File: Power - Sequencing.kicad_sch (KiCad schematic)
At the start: 0 parts

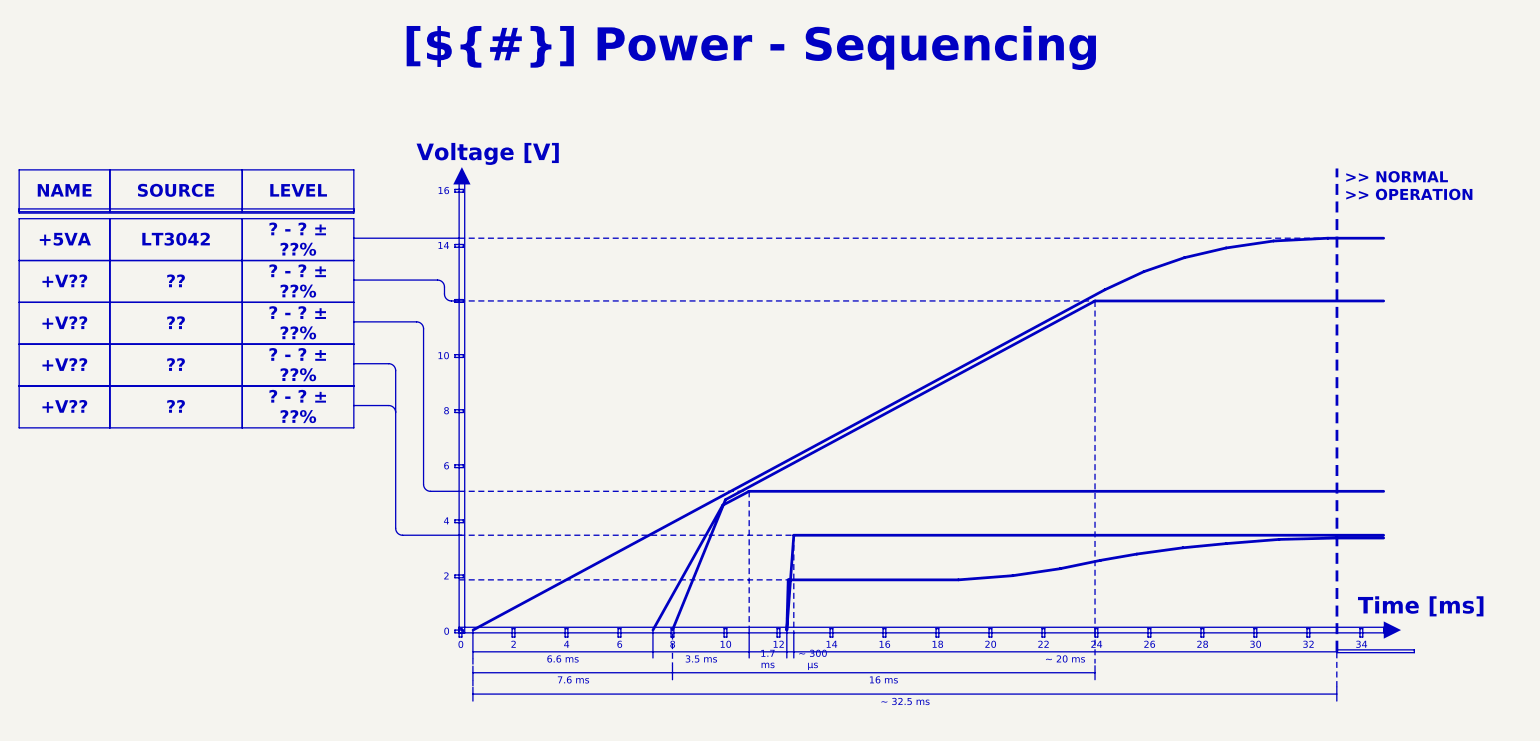
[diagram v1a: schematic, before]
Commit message: Fill template pages: block diagram, power sequencing, notes, revision history
Block Diagram and Power - Sequencing rebuilt from the real design (values computed
from the schematic); cover-page design notes, connector pinout notes, title-block
references; kicad-mcp-pro MCP config (.mcp.json).

Co-Authored-By: Claude Opus 5.5 <noreply@anthropic.com>
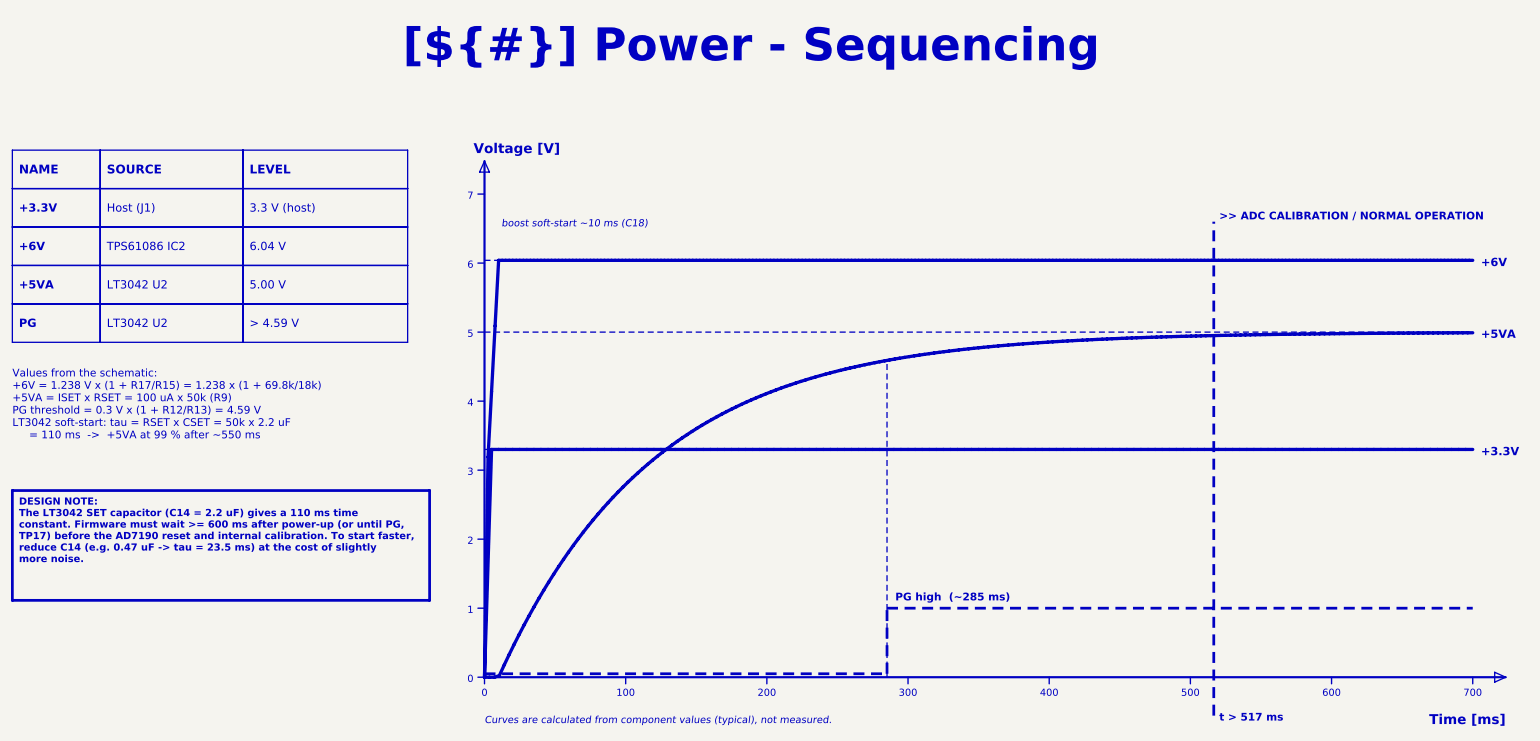
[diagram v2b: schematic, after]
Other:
- note added: "+3.3V"
- note added: "+5VA"
- note added: "+6V"
- note added: "0"
- note added: "1"
- note added: "100"
- note added: "2"
- note added: "200"
- note added: "3"
- note added: "300"
- note added: "4"
- note added: "400"
- note added: "5"
- note added: "500"
- note added: "6"
- note added: "600"
- note added: "7"
- note added: "700"
- note added: ">> ADC CALIBRATION / NORMAL OPERATION"
- note added: "Curves are calculated from component values (typical), not measured."
- note added: "PG high (~285 ms)"
- note added: "Values from the schematic: +6V = 1.238 V x (1 + R17/R15) = 1.238 x (1 + 69.8k/18k) +5VA = ISET x RSET = 100 uA x 50k (R9) PG threshold = 0.3 V x (1 + R12/R13) = 4.59 V LT3042 soft-start: tau = RSET x CSET = 50k x 2.2 uF = 110 ms -> +5VA at 99 % after ~550 ms"
- note added: "boost soft-start ~10 ms (C18)"
- note added: "t > 517 ms"
- note removed: ">> NORMAL >> OPERATION"
